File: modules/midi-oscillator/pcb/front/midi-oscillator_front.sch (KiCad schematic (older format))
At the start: 45 parts, among them J1 AudioJack3, J2 Conn_01x04, J3 CH1, J4 CH2, J5 CH3, J6 CH4, J7 Conn_01x14, SW1 Rotary_Encoder_Switch, U1 6N137, U2 TL071, U3 TL074

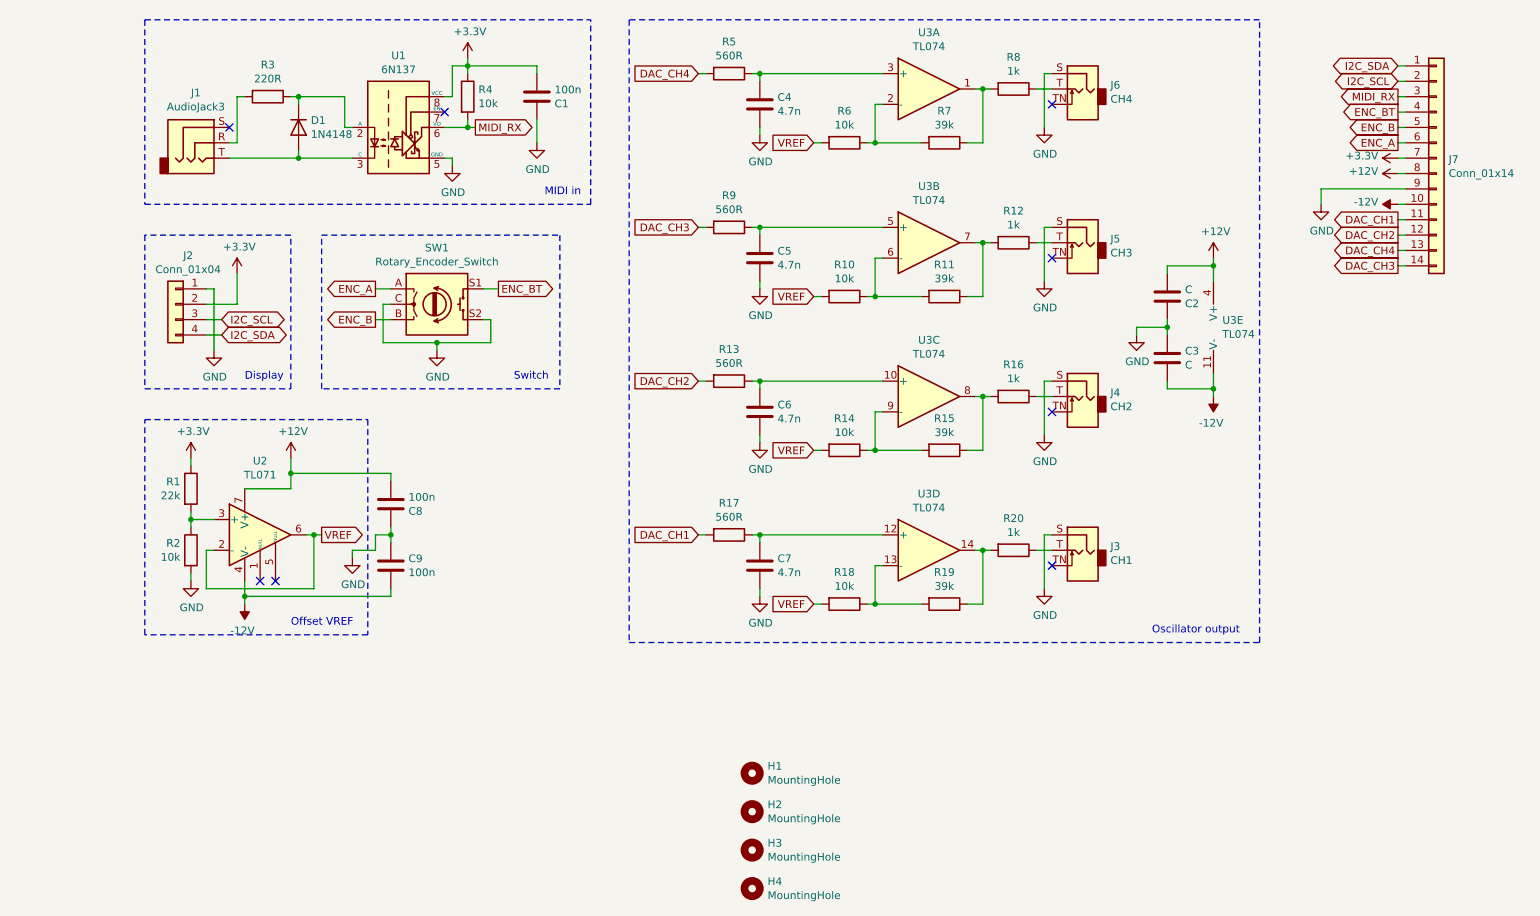
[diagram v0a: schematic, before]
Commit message: modules: midi-oscilator: pcb: fix schematics and add page metadata
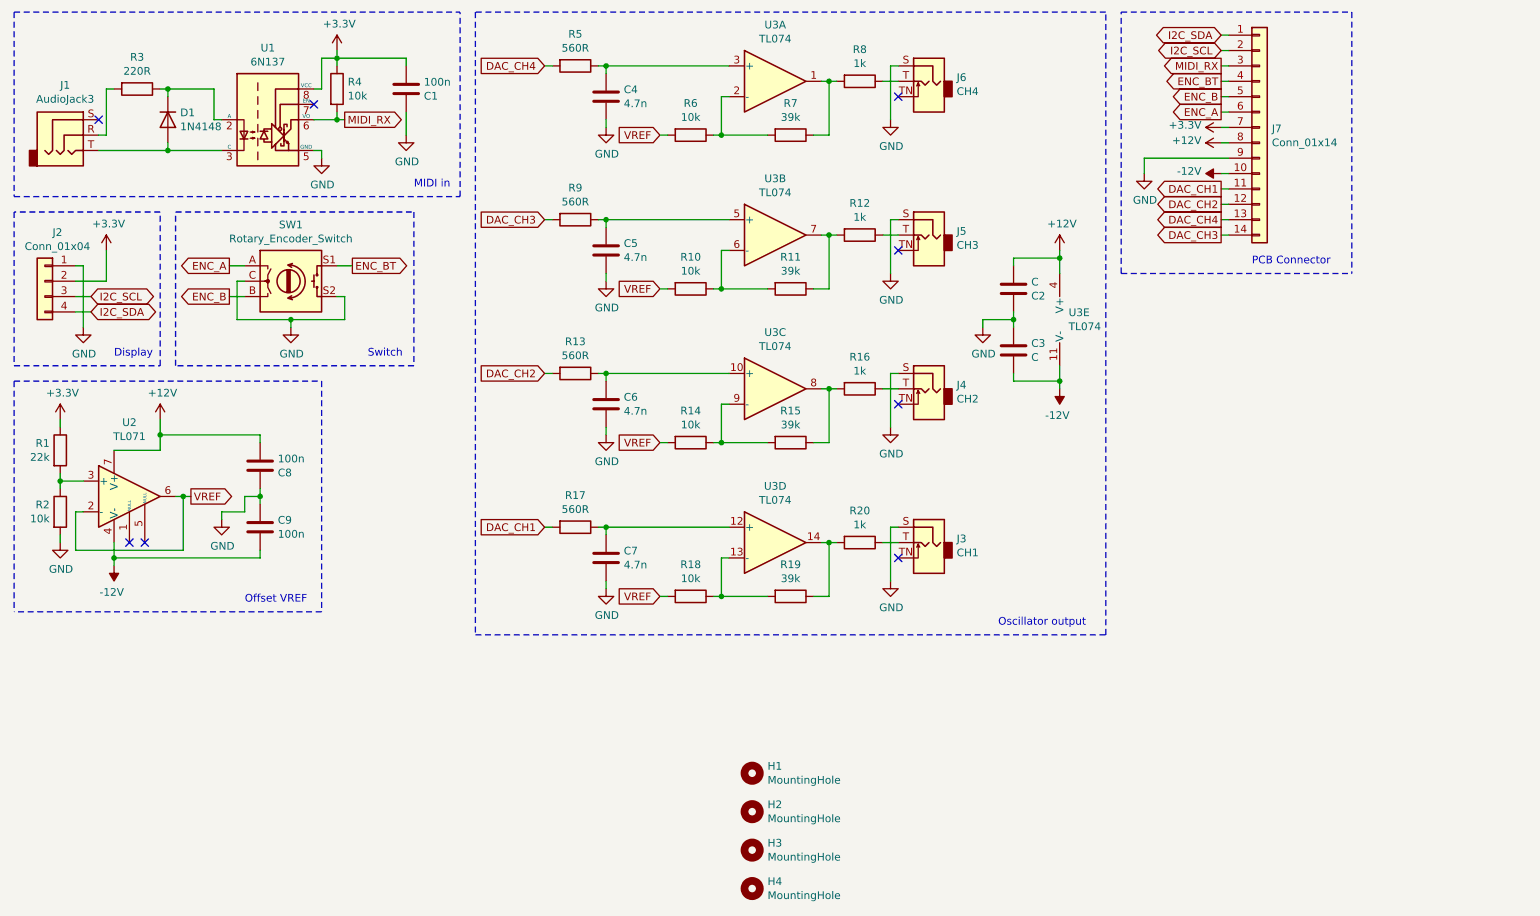
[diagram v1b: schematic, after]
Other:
- note added: "PCB Connector"
- moved on the sheet: C1, C2, C3, C4, C5, C6, C7, C8, C9, D1, J1, J2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

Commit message: modules: midi-oscillator: schematic improvements, added pdf
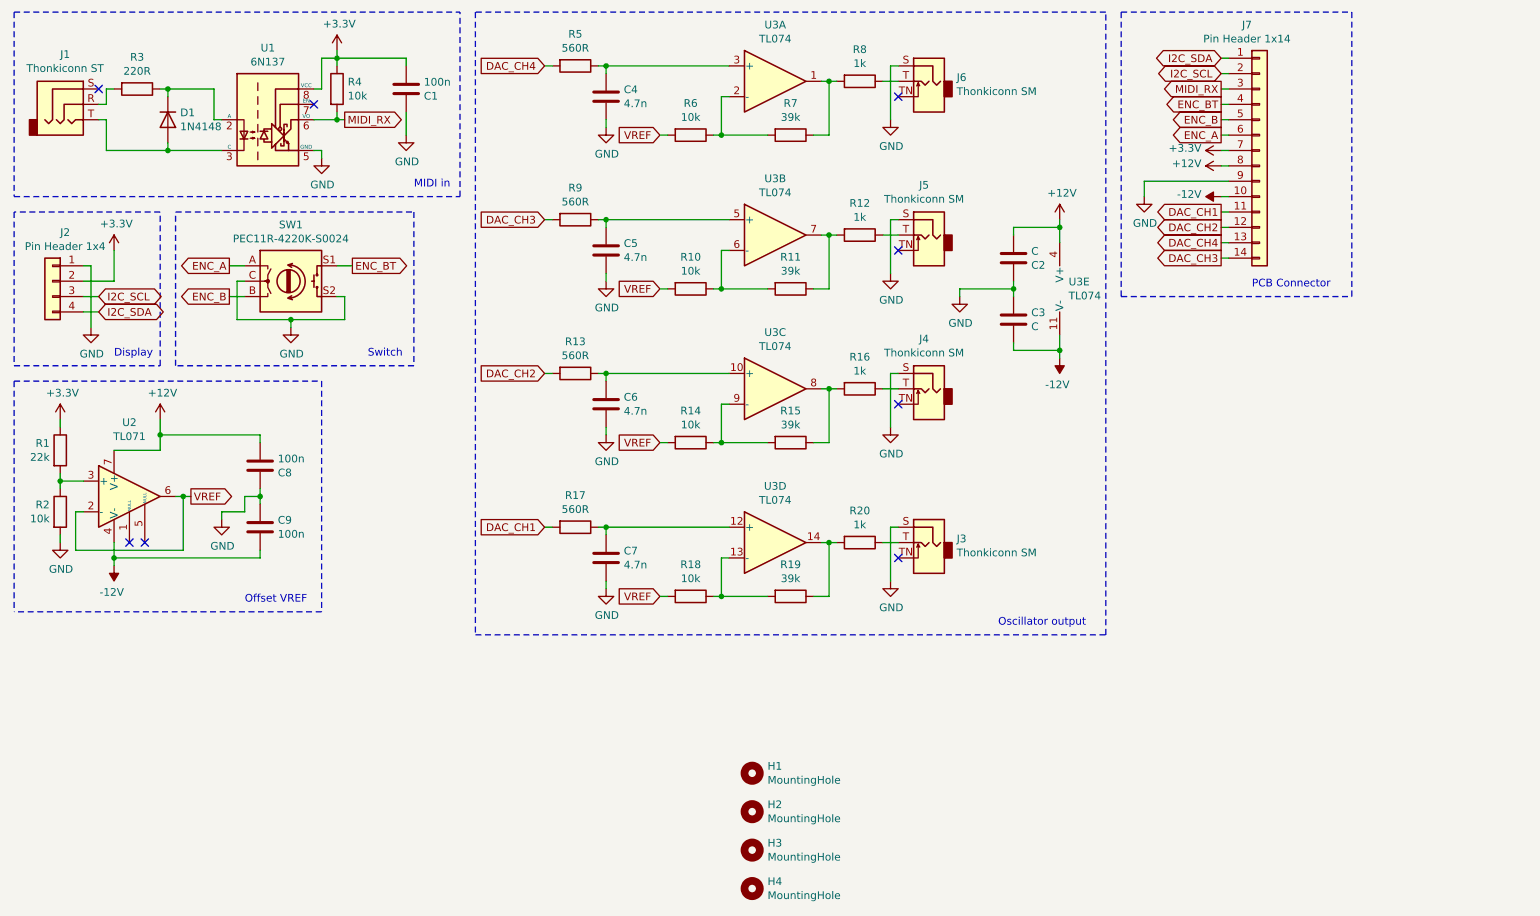
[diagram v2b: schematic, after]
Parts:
- J1: value AudioJack3 -> Thonkiconn ST
- J2: value Conn_01x04 -> Pin Header 1x4
- J3: value CH1 -> Thonkiconn SM
- J4: value CH2 -> Thonkiconn SM
- J5: value CH3 -> Thonkiconn SM
- J6: value CH4 -> Thonkiconn SM
- J7: value Conn_01x14 -> Pin Header 1x14
- SW1: value Rotary_Encoder_Switch -> PEC11R-4220K-S0024
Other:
- moved on the sheet: C2, C3, J1, J2, J7, U3E
